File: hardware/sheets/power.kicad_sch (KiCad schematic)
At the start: 24 parts, among them J1 USB_C_Receptacle, U1 CH224K, U2 TPS563200

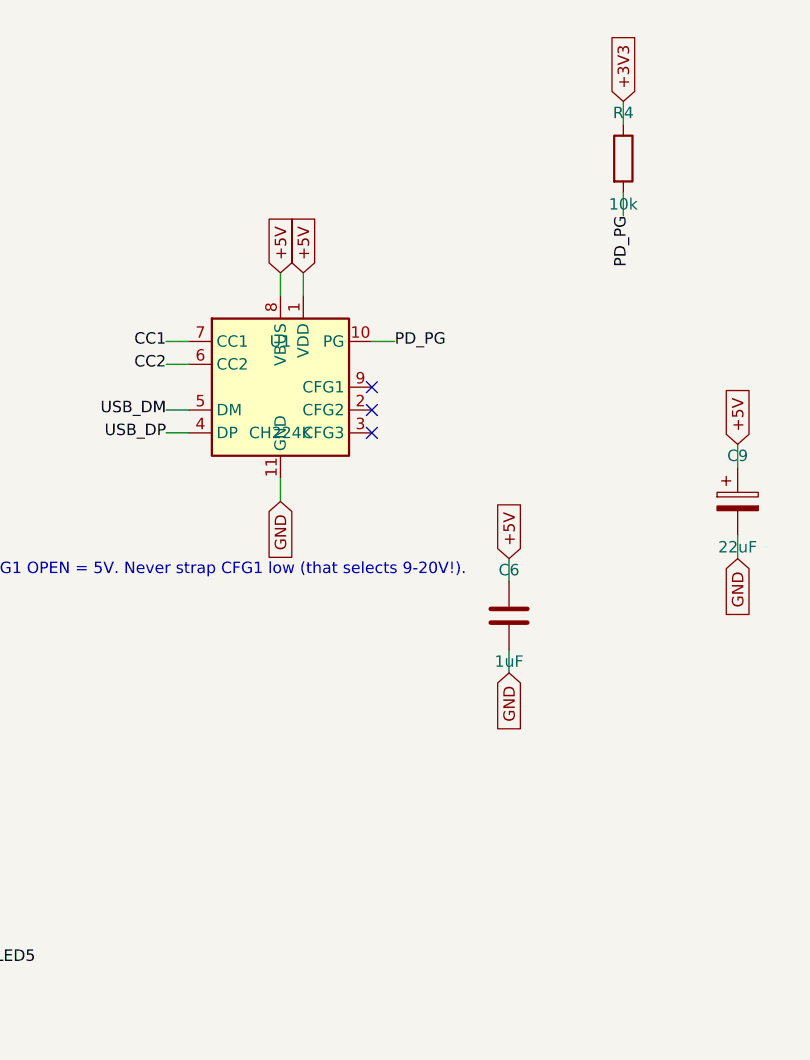
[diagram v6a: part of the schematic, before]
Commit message: Design-review fixes: reset parking, IRQ8 off the header, analog cleanups
Netlist-wide review sweep. IRQ8 leaves the 60-pin ISA header (pin 15 is a
second GND return; the on-board RTC owns IRQ8 exclusively, so its push-pull
drive is now correct by construction). Bus MCU Hi-Z parking completed:
~CPURESET pulled low (V20 held in reset while the MCU is unprogrammed),
~DACK1/~REFRESH parked deasserted, DRQ1 idled low. Supervisor 12 MHz crystal
damping R actually in series now (was parallel-to-nothing), plus a second
USBLC6 so both prog-port SW2 positions are ESD-protected. Audio: 0.5x PG
summing (MCP6002 headroom), 100k LINE bleed, unit B parked as a follower --
and the SUM stub moved off pin 5's row, where wiring unit B would have
silently merged SUM into VREF. CH224K VDD fed through 1k per the WCH ref
design. VGA blue ladder rescaled 1k/510 -> 820/470 (was ~12% blue-deficient).
Spare CMOS gate inputs grounded uniformly (cpu_core/rtc/storage); UART_RXD
pulled up (SIN idles at mark with JP1 open); dead pins/parts dropped
(com_port CLK, parallel RESET_DRV, storage R3). Bus CLK fixed at 7.16 MHz
logged as a decision. New passives mapped to JLC basic parts in parts.py.

Co-Authored-By: Claude Fable 5 <noreply@anthropic.com>
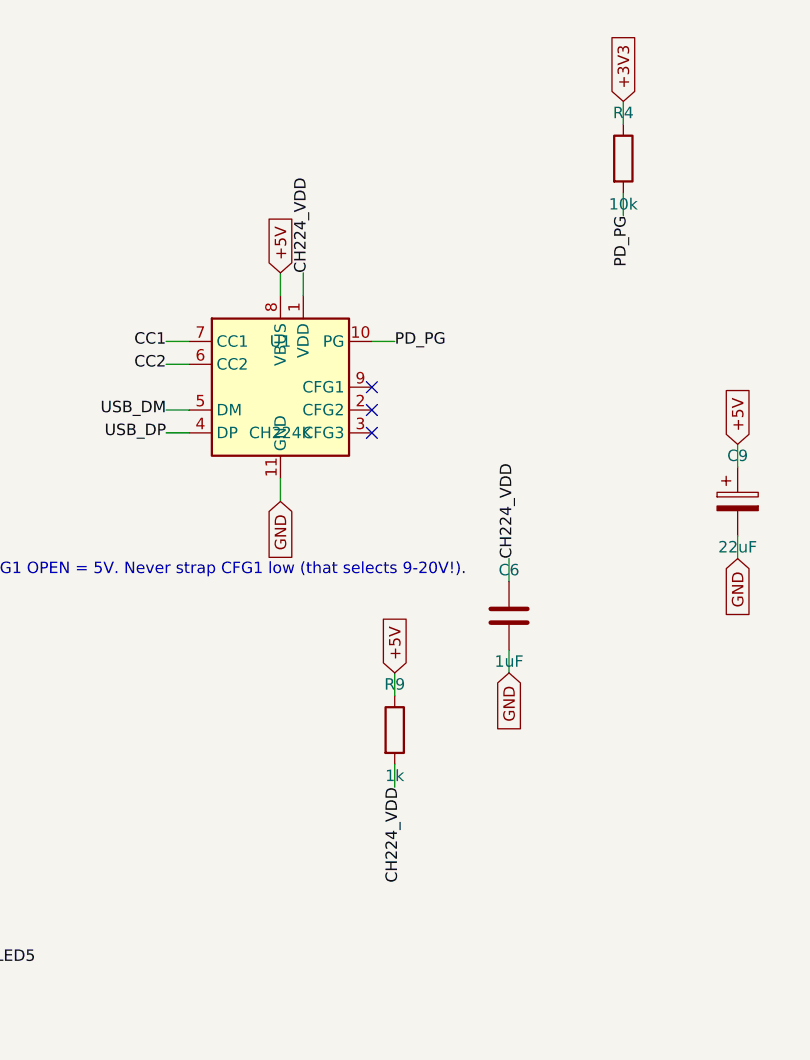
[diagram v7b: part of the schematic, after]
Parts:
- removed C5: 100nF, symbol Device:C
- removed R4: 10k, symbol Device:R
- added D2: 3V3, symbol Device:LED
- added R9: 1k, symbol Device:R
- added U2: TPS563200, symbol Regulator_Switching:TPS563200
- C1: renamed from C2; value 100nF -> 22uF; symbol Device:C -> Device:C_Polarized; LCSC Part Num C14663 -> C12891
- C2: renamed from U2; value TPS563200 -> 100nF; symbol Regulator_Switching:TPS563200 -> Device:C; LCSC Part Num C97253 -> C14663
- C3: renamed from C4; value 100nF -> 22uF; symbol Device:C -> Device:C_Polarized; LCSC Part Num C14663 -> C12891
- C4: renamed from C7; value 22uF -> 100nF; symbol Device:C_Polarized -> Device:C; LCSC Part Num C12891 -> C14663
- C5: renamed from L1; value 2.2uH -> 100nF; symbol Device:L -> Device:C; LCSC Part Num C602029 -> C14663
- C6: renamed from C1; value 22uF -> 1uF; symbol Device:C_Polarized -> Device:C; LCSC Part Num C12891 -> C15849
- C7: renamed from C8; value 10uF -> 22uF; symbol Device:C -> Device:C_Polarized; LCSC Part Num C15850 -> C12891
- C8: renamed from C9; value 22uF -> 10uF; symbol Device:C_Polarized -> Device:C; LCSC Part Num C12891 -> C15850
- C9: renamed from R7; value 1k -> 22uF; symbol Device:R -> Device:C_Polarized; LCSC Part Num C21190 -> C12891
- D1: renamed from R8; value 1k -> 5V; symbol Device:R -> Device:LED; LCSC Part Num C21190 -> C2286
- L1: renamed from R5; value 33k -> 2.2uH; symbol Device:R -> Device:L; LCSC Part Num C4216 -> C602029
- R4: renamed from C6; value 1uF -> 10k; symbol Device:C -> Device:R; LCSC Part Num C15849 -> C25804
- R5: renamed from R6; value 10k -> 33k; LCSC Part Num C25804 -> C4216
- R6: renamed from C3; value 22uF -> 10k; symbol Device:C_Polarized -> Device:R; LCSC Part Num C12891 -> C25804
- R7: renamed from D1; value 5V -> 1k; symbol Device:LED -> Device:R; LCSC Part Num C2286 -> C21190
- R8: renamed from D2; value 3V3 -> 1k; symbol Device:LED -> Device:R; LCSC Part Num C2286 -> C21190
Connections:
- net +3V3: now also C7.1, L1.2, R4.1, R5.1, R8.1; no longer C5.2, D1.1, L1.1, R6.1
- net +5V: now also C2.1, R7.1, R9.1, U2.3 (VIN), U2.5 (EN); no longer C2.3 (VIN), C2.5 (EN), C6.1, C7.1, R4.1, U1.1 (VDD)
- net BOOT: now also C5.1, U2.6 (VBST); no longer C2.6 (VBST)
- net FB: now also R5.2, R6.1, U2.4 (VFB); no longer C2.4 (VFB), L1.2, R5.1
- net GND: now also C2.2, C9.2, D1.1 (K), D2.1 (K), U2.1 (GND); no longer C2.1 (GND), R4.2, R5.2, R7.1 (K), R8.1 (K)
- net LED33: now also D2.2 (A); no longer D1.2
- net LED5: now also D1.2 (A); no longer C9.2
- net PD_PG: now also R4.2
- net SW: now also C5.2, L1.1, U2.2 (SW); no longer C2.2 (SW), C5.1
- new net CH224_VDD: C6.1, R9.2, U1.1 (VDD)
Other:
- moved on the sheet: R5
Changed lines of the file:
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@@
+		)
+	)
+	(label "CH224_VDD"
+		(at 142.24 152.4 90)
+		(effects
+			(font
+				(size 1.27 1.27)
+			)
+		)
+	)
+	(wire
+		(pts
+			(xy 152.4 199.39)
+			(xy 152.4 196.85)
+		)
+		(stroke
+			(width 0)
+			(type default)
 		)
 	)
 	(global_label "+5V"
 		(shape input)
-		(at 142.24 152.4 90)
+		(at 152.4 196.85 90)
+		(effects
+			(font
+				(size 1.27 1.27)
+			)
+		)
+	)
+	(wire
+		(pts
+			(xy 152.4 207.01)
+			(xy 152.4 209.55)
+		)
+		(stroke
+			(width 0)
+			(type default)
+		)
+	)
+	(label "CH224_VDD"
+		(at 152.4 209.55 270)
 		(effects
 			(font
@@
 		)
 	)
-	(global_label "+5V"
-		(shape input)
+	(label "CH224_VDD"
 		(at 165.1 184.15 90)
 		(effects
@@
 		(instances
 			(project "mini-xt"
-				(path "/26736c46-8b40-5460-874f-03596d17270c/d4837c83-dea4-50e2-90c8-39c05f336f73"
+				(path "/26736c46-8b40-5460-874f-03596d17270c/68f49a9c-4c78-5695-9186-0a02271fa638"
 					(reference "J901")
 					(unit 1)
@@
 		(instances
 			(project "mini-xt"
-				(path "/26736c46-8b40-5460-874f-03596d17270c/d4837c83-dea4-50e2-90c8-39c05f336f73"
+				(path "/26736c46-8b40-5460-874f-03596d17270c/68f49a9c-4c78-5695-9186-0a02271fa638"
 					(reference "R901")
 					(unit 1)
@@
 		(instances
 			(project "mini-xt"
-				(path "/26736c46-8b40-5460-874f-03596d17270c/d4837c83-dea4-50e2-90c8-39c05f336f73"
+				(path "/26736c46-8b40-5460-874f-03596d17270c/68f49a9c-4c78-5695-9186-0a02271fa638"
 					(reference "R902")
 					(unit 1)
@@
 		(instances
 			(project "mini-xt"
-				(path "/26736c46-8b40-5460-874f-03596d17270c/d4837c83-dea4-50e2-90c8-39c05f336f73"
+				(path "/26736c46-8b40-5460-874f-03596d17270c/68f49a9c-4c78-5695-9186-0a02271fa638"
 					(reference "F901")
 					(unit 1)
@@
 		(instances
 			(project "mini-xt"
-				(path "/26736c46-8b40-5460-874f-03596d17270c/d4837c83-dea4-50e2-90c8-39c05f336f73"
+				(path "/26736c46-8b40-5460-874f-03596d17270c/68f49a9c-4c78-5695-9186-0a02271fa638"
 					(reference "D903")
 					(unit 1)
@@
 		(instances
 			(project "mini-xt"
-				(path "/26736c46-8b40-5460-874f-03596d17270c/d4837c83-dea4-50e2-90c8-39c05f336f73"
+				(path "/26736c46-8b40-5460-874f-03596d17270c/68f49a9c-4c78-5695-9186-0a02271fa638"
 					(reference "U901")
+					(unit 1)
+				)
+			)
+		)
+	)
+	(symbol
+		(lib_id "Device:R")
+		(at 152.4 203.2 0)
+		(unit 1)
+		(exclude_from_sim no)
+		(in_bom yes)
+		(on_board yes)
+		(dnp no)
+		(fields_autoplaced yes)
+		(property "Reference" "R9"
+			(at 152.4 198.12 0)
+			(effects
+				(font
+					(size 1.27 1.27)
+				)
+			)
+		)
+		(property "Value" "1k"
+			(at 152.4 208.28 0)
+			(effects
+				(font
+					(size 1.27 1.27)
+				)
+			)
+		)
+		(property "Footprint" ""
+			(at 152.4 203.2 0)
+			(effects
+				(font
+					(size 1.27 1.27)
+				)
+				(hide yes)
+			)
+		)
+		(property "LCSC Part Num" "C21190"
+			(at 152.4 203.2 0)
+			(effects
+				(font
+					(size 1.27 1.27)
+				)
+				(hide yes)
+			)
+		)
+		(pin "1"
+		)
+		(pin "2"
+		)
+		(instances
+			(project "mini-xt"
+				(path "/26736c46-8b40-5460-874f-03596d17270c/68f49a9c-4c78-5695-9186-0a02271fa638"
+					(reference "R909")
 					(unit 1)
 				)
@@
 		(instances
 			(project "mini-xt"
-				(path "/26736c46-8b40-5460-874f-03596d17270c/d4837c83-dea4-50e2-90c8-39c05f336f73"
+				(path "/26736c46-8b40-5460-874f-03596d17270c/68f49a9c-4c78-5695-9186-0a02271fa638"
 					(reference "R904")
 					(unit 1)
@@
 		(instances
 			(project "mini-xt"
-				(path "/26736c46-8b40-5460-874f-03596d17270c/d4837c83-dea4-50e2-90c8-39c05f336f73"
+				(path "/26736c46-8b40-5460-874f-03596d17270c/68f49a9c-4c78-5695-9186-0a02271fa638"
 					(reference "C906")
 					(unit 1)
@@
 		(instances
 			(project "mini-xt"
-				(path "/26736c46-8b40-5460-874f-03596d17270c/d4837c83-dea4-50e2-90c8-39c05f336f73"
+				(path "/26736c46-8b40-5460-874f-03596d17270c/68f49a9c-4c78-5695-9186-0a02271fa638"
 					(reference "C901")
 					(unit 1)
@@
 		(instances
 			(project "mini-xt"
-				(path "/26736c46-8b40-5460-874f-03596d17270c/d4837c83-dea4-50e2-90c8-39c05f336f73"
+				(path "/26736c46-8b40-5460-874f-03596d17270c/68f49a9c-4c78-5695-9186-0a02271fa638"
 					(reference "C902")
 					(unit 1)
@@
 		(instances
 			(project "mini-xt"
-				(path "/26736c46-8b40-5460-874f-03596d17270c/d4837c83-dea4-50e2-90c8-39c05f336f73"
+				(path "/26736c46-8b40-5460-874f-03596d17270c/68f49a9c-4c78-5695-9186-0a02271fa638"
 					(reference "U902")
 					(unit 1)
@@
 		(instances
 			(project "mini-xt"
-				(path "/26736c46-8b40-5460-874f-03596d17270c/d4837c83-dea4-50e2-90c8-39c05f336f73"
+				(path "/26736c46-8b40-5460-874f-03596d17270c/68f49a9c-4c78-5695-9186-0a02271fa638"
 					(reference "C905")
 					(unit 1)
@@
 		(instances
 			(project "mini-xt"
-				(path "/26736c46-8b40-5460-874f-03596d17270c/d4837c83-dea4-50e2-90c8-39c05f336f73"
+				(path "/26736c46-8b40-5460-874f-03596d17270c/68f49a9c-4c78-5695-9186-0a02271fa638"
 					(reference "L901")
 					(unit 1)
@@
 		(instances
 			(project "mini-xt"
-				(path "/26736c46-8b40-5460-874f-03596d17270c/d4837c83-dea4-50e2-90c8-39c05f336f73"
+				(path "/26736c46-8b40-5460-874f-03596d17270c/68f49a9c-4c78-5695-9186-0a02271fa638"
 					(reference "R905")
 					(unit 1)
@@
 		(instances
 			(project "mini-xt"
-				(path "/26736c46-8b40-5460-874f-03596d17270c/d4837c83-dea4-50e2-90c8-39c05f336f73"
+				(path "/26736c46-8b40-5460-874f-03596d17270c/68f49a9c-4c78-5695-9186-0a02271fa638"
 					(reference "R906")
 					(unit 1)
@@
 		(instances
 			(project "mini-xt"
-				(path "/26736c46-8b40-5460-874f-03596d17270c/d4837c83-dea4-50e2-90c8-39c05f336f73"
+				(path "/26736c46-8b40-5460-874f-03596d17270c/68f49a9c-4c78-5695-9186-0a02271fa638"
 					(reference "C903")
 					(unit 1)
@@
 		(instances
 			(project "mini-xt"
-				(path "/26736c46-8b40-5460-874f-03596d17270c/d4837c83-dea4-50e2-90c8-39c05f336f73"
+				(path "/26736c46-8b40-5460-874f-03596d17270c/68f49a9c-4c78-5695-9186-0a02271fa638"
 					(reference "C904")
 					(unit 1)
@@
 		(instances
 			(project "mini-xt"
-				(path "/26736c46-8b40-5460-874f-03596d17270c/d4837c83-dea4-50e2-90c8-39c05f336f73"
+				(path "/26736c46-8b40-5460-874f-03596d17270c/68f49a9c-4c78-5695-9186-0a02271fa638"
 					(reference "C907")
 					(unit 1)
@@
 		(instances
 			(project "mini-xt"
-				(path "/26736c46-8b40-5460-874f-03596d17270c/d4837c83-dea4-50e2-90c8-39c05f336f73"
+				(path "/26736c46-8b40-5460-874f-03596d17270c/68f49a9c-4c78-5695-9186-0a02271fa638"
 					(reference "C908")
 					(unit 1)
@@
 		(instances
 			(project "mini-xt"
-				(path "/26736c46-8b40-5460-874f-03596d17270c/d4837c83-dea4-50e2-90c8-39c05f336f73"
+				(path "/26736c46-8b40-5460-874f-03596d17270c/68f49a9c-4c78-5695-9186-0a02271fa638"
 					(reference "C909")
 					(unit 1)
@@
 		(instances
 			(project "mini-xt"
-				(path "/26736c46-8b40-5460-874f-03596d17270c/d4837c83-dea4-50e2-90c8-39c05f336f73"
+				(path "/26736c46-8b40-5460-874f-03596d17270c/68f49a9c-4c78-5695-9186-0a02271fa638"
 					(reference "R907")
 					(unit 1)
@@
 		(instances
 			(project "mini-xt"
-				(path "/26736c46-8b40-5460-874f-03596d17270c/d4837c83-dea4-50e2-90c8-39c05f336f73"
+				(path "/26736c46-8b40-5460-874f-03596d17270c/68f49a9c-4c78-5695-9186-0a02271fa638"
 					(reference "D901")
 					(unit 1)
@@
 		(instances
 			(project "mini-xt"
-				(path "/26736c46-8b40-5460-874f-03596d17270c/d4837c83-dea4-50e2-90c8-39c05f336f73"
+				(path "/26736c46-8b40-5460-874f-03596d17270c/68f49a9c-4c78-5695-9186-0a02271fa638"
 					(reference "R908")
 					(unit 1)
@@
 		(instances
 			(project "mini-xt"
-				(path "/26736c46-8b40-5460-874f-03596d17270c/d4837c83-dea4-50e2-90c8-39c05f336f73"
+				(path "/26736c46-8b40-5460-874f-03596d17270c/68f49a9c-4c78-5695-9186-0a02271fa638"
 					(reference "D902")
 					(unit 1)
@@
 		(instances
 			(project "mini-xt"
-				(path "/26736c46-8b40-5460-874f-03596d17270c/d4837c83-dea4-50e2-90c8-39c05f336f73"
+				(path "/26736c46-8b40-5460-874f-03596d17270c/68f49a9c-4c78-5695-9186-0a02271fa638"
 					(reference "#FLG901")
 					(unit 1)
@@
 		(instances
 			(project "mini-xt"
-				(path "/26736c46-8b40-5460-874f-03596d17270c/d4837c83-dea4-50e2-90c8-39c05f336f73"
+				(path "/26736c46-8b40-5460-874f-03596d17270c/68f49a9c-4c78-5695-9186-0a02271fa638"
 					(reference "#FLG902")
 					(unit 1)
@@
 		(instances
 			(project "mini-xt"
-				(path "/26736c46-8b40-5460-874f-03596d17270c/d4837c83-dea4-50e2-90c8-39c05f336f73"
+				(path "/26736c46-8b40-5460-874f-03596d17270c/68f49a9c-4c78-5695-9186-0a02271fa638"
 					(reference "#FLG903")
 					(unit 1)
@@
 		(instances
 			(project "mini-xt"
-				(path "/26736c46-8b40-5460-874f-03596d17270c/d4837c83-dea4-50e2-90c8-39c05f336f73"
+				(path "/26736c46-8b40-5460-874f-03596d17270c/68f49a9c-4c78-5695-9186-0a02271fa638"
 					(reference "#FLG904")
 					(unit 1)
@@
 		(instances
 			(project "mini-xt"
-				(path "/26736c46-8b40-5460-874f-03596d17270c/d4837c83-dea4-50e2-90c8-39c05f336f73"
+				(path "/26736c46-8b40-5460-874f-03596d17270c/68f49a9c-4c78-5695-9186-0a02271fa638"
 					(reference "#PWR901")
 					(unit 1)
